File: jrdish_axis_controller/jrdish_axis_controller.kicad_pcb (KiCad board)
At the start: 4 copper layers, 85 x 80 mm, 168 parts, among them CN1 KF2EDGR-2.54-9P, CN10 KF2EDGR-2.54-4P, CN11 KF2EDGR-2.54-4P, CN12 KF2EDGR-2.54-2P, CN13 KF2EDGR-2.54-2P, CN2 KF2EDGR-2.54-6P, CN3 KF2EDGR-2.54-9P, CN4 KF2EDGR-2.54-6P, CN5 KF2EDGR-2.54-3P, CN6 KF2EDGR-2.54-2P, CN7 SM04B-SRSS-TB (LF)(SN), CN8 SM04B-SRSS-TB (LF)(SN), CN9 KF2EDGR-2.54-4P, J1 Conn_ARM_SWD_TagConnect_TC2030, M1 MountingHole_2.7mm_M2.5_ISO14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, Q1 AO3407A, Q2 AO3400A, Q3 2N7002, SW1 DSHP04TSGER, SW2 SS-12F49-G050, U1 STM32G474RET6, U2 ISOW1432BDFMR, U3 ISOW1432BDFMR, U4 MP2322GQH-Z, U5 LTC4311ISC6#TRPBF, U6 LM75BIMX-5/NOPB, U7 W25Q32JVSSIQ_C179173, U8 SP3232EEY-L/TR, X1 NX2016SA-16MHZ-EXS00A-CS07826

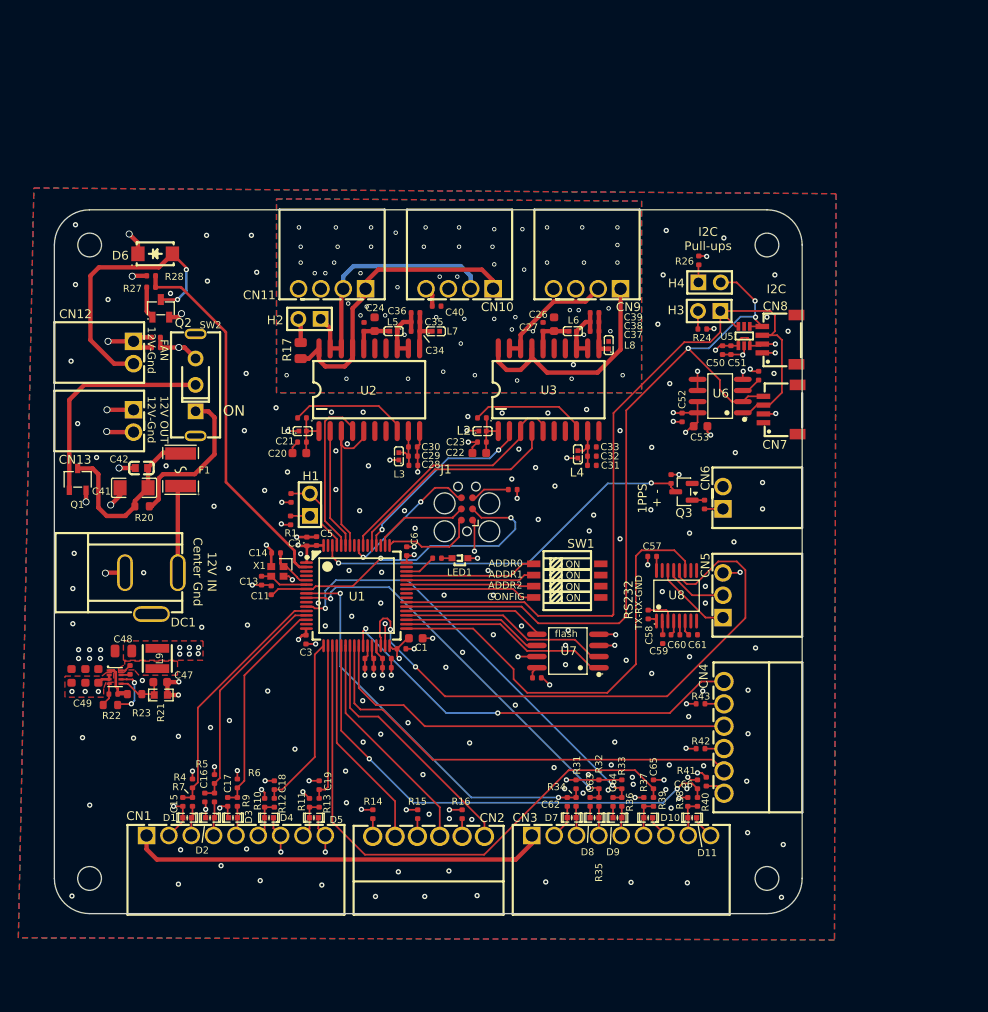
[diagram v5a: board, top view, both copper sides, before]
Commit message: RS485 isolated areas in place
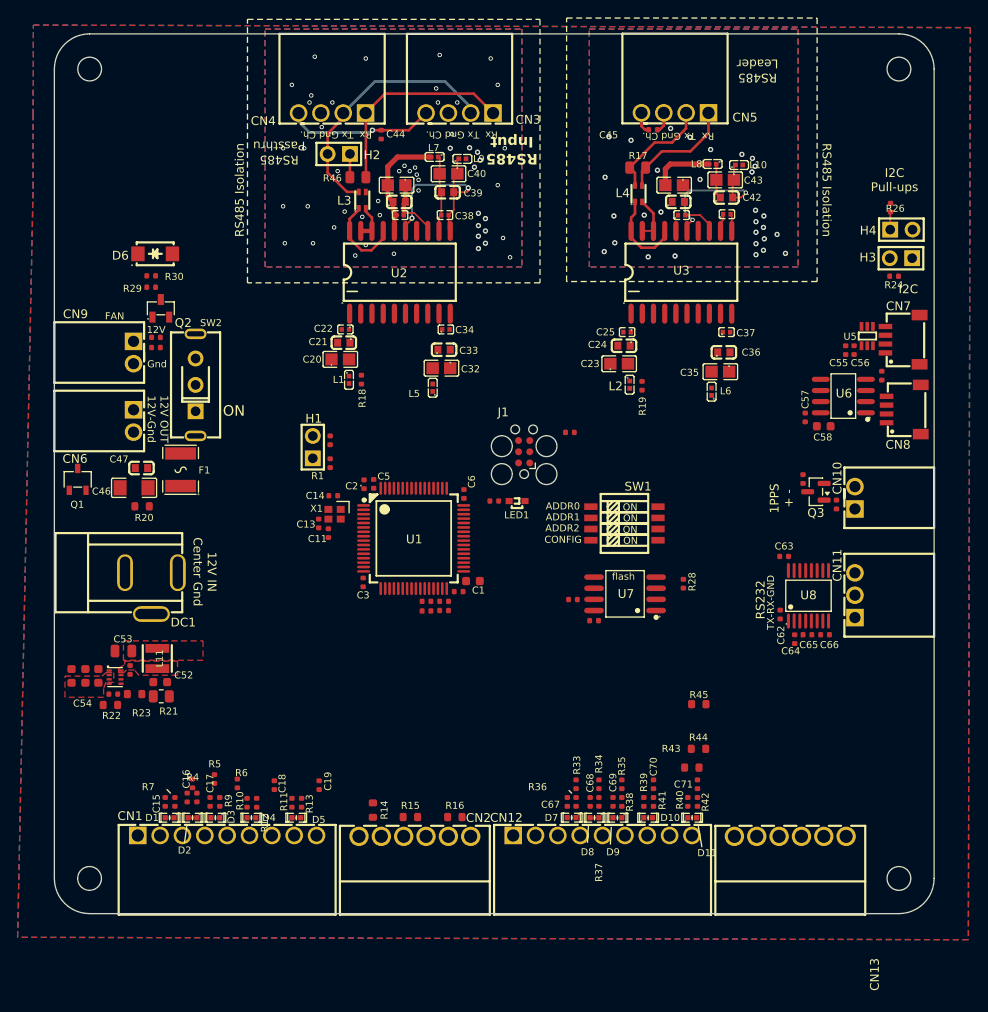
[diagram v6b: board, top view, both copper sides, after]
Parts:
- removed the CN4 at (191.5, 112.6)
- removed the R41 at (189.5, 117.6)
- removed the R42 at (188.8, 113.8)
- added C40: 10uF, MyParts:C0805, F.Cu at (160.2, 48.5)
- added C41: 10nF, MyParts:C0402, F.Cu at (191.8, 53.1)
- added C42: 1uF, MyParts:C0603, F.Cu at (191.8, 51.2)
- added C43: 10uF, MyParts:C0805, F.Cu at (191.7, 49.2)
- added C45: 10nF, PCM_JLCPCB:C_0402, F.Cu at (183.4, 43.5)
- added CN13: KF2EDGR-2.54-6P, MyParts:CONN-TH_KF2EDGR-2.54-6P, F.Cu at (199.1, 123.8)
- added L10: BLM15EX331SN1D, MyParts:L0402, F.Cu at (193.2, 47.5)
- added L3: Choke, MyParts:FILTER-SMD_4P-L2.0-W1.2-BL, F.Cu at (150.4, 51.5)
- added R27: 10kΩ, PCM_JLCPCB:R_0402, F.Cu at (174.3, 96.9)
- added R28: 10kΩ, PCM_JLCPCB:R_0402, F.Cu at (186.9, 95.1)
- added R44: 270Ω, PCM_JLCPCB:R_0603, F.Cu at (188.6, 113.9)
- added R45: 270Ω, PCM_JLCPCB:R_0603, F.Cu at (188.7, 108.8)
- added R46: 120Ω, PCM_JLCPCB:R_0805, F.Cu at (149.9, 48.9)
- C20: footprint PCM_JLCPCB:C_0603 -> MyParts:C0805
- C21, C27: value 100nF -> 1uF; footprint PCM_JLCPCB:C_0402 -> MyParts:C0603
- C22, C26: value 10uF -> .1uF; footprint PCM_JLCPCB:C_0603 -> MyParts:C0402
- C23: value 100nF -> 10uF; footprint PCM_JLCPCB:C_0402 -> MyParts:C0805
- C24: value 10uF -> 1uF; footprint PCM_JLCPCB:C_0603 -> MyParts:C0603
- C25: value 100nF -> .1uF; footprint PCM_JLCPCB:C_0402 -> MyParts:C0402
- C28, C31: value 10nF -> 10uF; footprint PCM_JLCPCB:C_0402 -> MyParts:C0805
- C29: value 1uF -> .1uF; footprint PCM_JLCPCB:C_0402 -> MyParts:C0402
- C30, C33, C36, C39: value 10nF -> 1uF; footprint PCM_JLCPCB:C_0402 -> MyParts:C0603
- C32, C35: value 1uF -> 10uF; footprint PCM_JLCPCB:C_0402 -> MyParts:C0805
- C34, C37: footprint PCM_JLCPCB:C_0402 -> MyParts:C0402
- C38: value 1uF -> 10nF; footprint PCM_JLCPCB:C_0402 -> MyParts:C0402
- L4: value BLM15EX331SN1D -> Choke; footprint MyParts:L0402 -> MyParts:FILTER-SMD_4P-L2.0-W1.2-BL
- R14, R15, R16, R43: value 330Ω -> 270Ω; footprint PCM_JLCPCB:R_0402 -> PCM_JLCPCB:R_0603
- R21: value 976Ω -> 976kΩ; footprint MyParts:R0603 -> Resistor_SMD:R_0805_2012Metric
- moved R17 43.6 mm to (181.7, 47.8), turned to 180 degrees
- moved C30 41.1 mm to (186.3, 51.7)
- moved C29 41.0 mm to (186.7, 53.2)
- moved C36 35.3 mm to (191.5, 68.8)
- moved C35 35.1 mm to (191.1, 71.0), turned to 180 degrees
- moved C31 33.2 mm to (185.8, 49.8), turned to 180 degrees
- moved C28 31.9 mm to (154.3, 49.8), turned to 180 degrees
- moved L4 30.4 mm to (181.8, 50.8), turned to 0 degrees
- moved C25 29.9 mm to (180.5, 66.5), turned to 180 degrees
- moved C24 28.5 mm to (180.2, 68.0), turned to 180 degrees
- moved M1 25.0 mm to (211.4, 36.6)
- moved L8 23.7 mm to (190.2, 47.4), turned to 180 degrees
- moved H4 22.6 mm to (211.7, 54.9)
- moved H3 22.6 mm to (211.6, 58.1)
- moved R24 22.6 mm to (210.8, 60.1)
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- renumbered C40 to C44, C41 to C46, C42 to C47, C43 to C48, C44 to C49, C45 to C50, C46 to C51, C47 to C52, C48 to C53, C49 to C54, C50 to C55, C51 to C56, C52 to C57, C53 to C58, C54 to C59, C55 to C60, C56 to C61, C58 to C62, C57 to C63, C59 to C64, C60 to C65, C61 to C66, C62 to C67, C63 to C68, C64 to C69, C65 to C70, C66 to C71, CN6 to CN10, CN5 to CN11, CN3 to CN12, CN10 to CN3, CN11 to CN4, CN9 to CN5, CN13 to CN6, CN8 to CN7, CN7 to CN8, CN12 to CN9, L9 to L11, L3 to L5, L5 to L7, L7 to L9, R27 to R29, R28 to R30, R29 to R31, R30 to R32, R31 to R33, R32 to R34, R33 to R35, R34 to R36, R35 to R37, R36 to R38, R37 to R39, R38 to R40, R39 to R41, R40 to R42
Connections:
- C20 pad 1: Net-(U2-VIO) -> GND
- C20 pad 2: GND -> Net-(U2-VIO)
- C22 pad 1: Net-(U3-VIO) -> Net-(U2-VIO)
- C23 pad 1: Net-(U3-VIO) -> GND
- C23 pad 2: GND -> Net-(U3-VIO)
- C24 pad 1: Net-(U2-VISOIN) -> Net-(U3-VIO)
- C24 pad 2: RS485_GND -> GND
- C25 pad 1: Net-(U2-VISOIN) -> Net-(U3-VIO)
- C25 pad 2: RS485_GND -> GND
- C26 pad 1: Net-(U3-VISOIN) -> Net-(U2-VISOIN)
- C26 pad 2: RS485_GND -> RS485_1_GND
- C27 pad 1: Net-(U3-VISOIN) -> Net-(U2-VISOIN)
- C27 pad 2: RS485_GND -> RS485_1_GND
- C28 pad 1: Net-(U2-VDD) -> RS485_1_GND
- C28 pad 2: GND -> Net-(U2-VISOIN)
- C29 pad 1: Net-(U2-VDD) -> Net-(U3-VISOIN)
- C29 pad 2: GND -> RS485_2_GND
- C30 pad 1: Net-(U2-VDD) -> Net-(U3-VISOIN)
- C30 pad 2: GND -> RS485_2_GND
- C31 pad 1: Net-(U3-VDD) -> RS485_2_GND
- C31 pad 2: GND -> Net-(U3-VISOIN)
- C32 pad 1: Net-(U3-VDD) -> GND
- C32 pad 2: GND -> Net-(U2-VDD)
- C33 pad 1: Net-(U3-VDD) -> Net-(U2-VDD)
- C34 pad 1: Net-(U2-MODE) -> Net-(U2-VDD)
- C34 pad 2: Net-(U2-GND2) -> GND
- C35 pad 1: Net-(U2-MODE) -> GND
- C35 pad 2: Net-(U2-GND2) -> Net-(U3-VDD)
- C36 pad 1: Net-(U2-MODE) -> Net-(U3-VDD)
- C36 pad 2: Net-(U2-GND2) -> GND
- C37 pad 1: Net-(U3-MODE) -> Net-(U3-VDD)
- C37 pad 2: Net-(U3-GND2) -> GND
- C38 pad 1: Net-(U3-MODE) -> Net-(U2-VISOOUT)
- C38 pad 2: Net-(U3-GND2) -> Net-(U2-GISOIN)
- C39 pad 1: Net-(U3-MODE) -> Net-(U2-VISOOUT)
- C39 pad 2: Net-(U3-GND2) -> Net-(U2-GISOIN)
- C44 pad 1: RS485_GND -> RS485_1_GND
- C44 pad 2: /RS485/RS485_CHASSIS -> /RS485/RS485_1_CHASSIS
- C59 pad 2: Net-(U7-VCC) -> GND
- C63 pad 2: Net-(U8-VCC) -> GND
- CN3 pad 1: /RS485/RS485_1_TX -> /RS485/RS485_1_RX
- CN3 pad 2: /RS485/RS485_1_RX -> /RS485/RS485_1_TX
- CN3 pad 3: RS485_GND -> RS485_1_GND
- CN3 pad 4: /RS485/RS485_CHASSIS -> /RS485/RS485_1_CHASSIS
- CN4 pad 1: /RS485/RS485_1_TX -> /RS485/RS485_1_RX
- CN4 pad 2: /RS485/RS485_1_RX -> /RS485/RS485_1_TX
- CN4 pad 3: RS485_GND -> RS485_1_GND
- CN4 pad 4: unconnected-(CN11-Pad4) -> /RS485/RS485_1_CHASSIS
- CN5 pad 1: /RS485/RS485_2_TX -> /RS485/RS485_2_RX
- CN5 pad 2: /RS485/RS485_2_RX -> /RS485/RS485_2_TX
- CN5 pad 3: RS485_GND -> RS485_2_GND
- CN5 pad 4: unconnected-(CN9-Pad4) -> /RS485/RS485_2_CHASSIS
- H2 pad 1: /RS485/RS485_1_RX -> Net-(H2-Pad1)
- H2 pad 2: Net-(H2-Pad2) -> /RS485/RS485_1_TX
- L1 pad 1: 3V3 -> Net-(U2-VIO)
- L1 pad 2: Net-(U2-VIO) -> 3V3
- L2 pad 1: 3V3 -> Net-(U3-VIO)
- L2 pad 2: Net-(U3-VIO) -> 3V3
- L4 pad 1: 3V3 -> Net-(U3-A)
- L4 pad 2: Net-(U3-VDD) -> Net-(U3-B)
- L6 pad 1: Net-(U3-MODE) -> 3V3
- L6 pad 2: Net-(U3-VISOIN) -> Net-(U3-VDD)
- L7 pad 1: Net-(U2-MODE) -> Net-(U2-VISOOUT)
- L8 pad 1: Net-(U3-GND2) -> Net-(U3-VISOOUT)
- L8 pad 2: RS485_GND -> Net-(U3-VISOIN)
- L9 pad 1: Net-(U2-GND2) -> Net-(U2-GISOIN)
- L9 pad 2: RS485_GND -> RS485_1_GND
- Q1 pad 2: 12V -> /Power/12V_IN_FUSED
- Q1 pad 3: /Power/12V_IN_FUSED -> 12V
- R17 pad 1: Net-(H2-Pad2) -> /RS485/RS485_2_RX
- R17 pad 2: /RS485/RS485_1_TX -> /RS485/RS485_2_TX
- R21 pad 1: Net-(U4-FB) -> 3V3
- R21 pad 2: 3V3 -> Net-(U4-FB)
- U2 pad 11: Net-(U2-GND2) -> Net-(U2-GISOIN)
- U2 pad 12: Net-(U2-MODE) -> Net-(U2-VISOOUT)
- U2 pad 13: Net-(U2-MODE) -> RS485_1_GND
- U2 pad 15: RS485_GND -> Net-(U2-GISOIN)
- U2 pad 17: /RS485/RS485_1_TX -> Net-(U2-A)
- U2 pad 18: /RS485/RS485_1_RX -> Net-(U2-B)
- U2 pad 19: /RS485/RS485_1_RX -> Net-(U2-B)
- U2 pad 20: /RS485/RS485_1_TX -> Net-(U2-A)
- U3 pad 11: Net-(U3-GND2) -> Net-(U3-GISOIN)
- U3 pad 12: Net-(U3-MODE) -> Net-(U3-VISOOUT)
- U3 pad 13: Net-(U3-MODE) -> RS485_2_GND
- U3 pad 15: RS485_GND -> Net-(U3-GISOIN)
- U3 pad 17: /RS485/RS485_2_TX -> Net-(U3-A)
- U3 pad 18: /RS485/RS485_2_RX -> Net-(U3-B)
- U3 pad 19: /RS485/RS485_2_RX -> Net-(U3-B)
- U3 pad 20: /RS485/RS485_2_TX -> Net-(U3-A)
- U7 pad 3: GND -> Net-(U7-WP#(IO2))
- U7 pad 7: GND -> Net-(U7-I03)
- U7 pad 8: Net-(U7-VCC) -> 3V3
- U8 pad 16: Net-(U8-VCC) -> 3V3
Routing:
- net GND: track 111.4 -> 0.00 mm, vias 193 -> 0
- net SDA_MCU: track 91.9 -> 0.00 mm
- net SCL_MCU: track 89.9 -> 0.00 mm, vias 3 -> 0
- net 3V3: track 78.1 -> 0.00 mm, vias 46 -> 0
- net RS232_RX_MCU: track 68.7 -> 0.00 mm, vias 2 -> 0
- net 12V: track 64.0 -> 0.00 mm, vias 7 -> 0
- net LIMIT2_SW1_MCU: track 63.9 -> 0.00 mm
- net LIMIT2_SW2_MCU: track 55.7 -> 0.00 mm, vias 2 -> 0
- net PUL2_MCU: track 51.7 -> 0.00 mm
- net RS232_TX_MCU: track 50.9 -> 0.00 mm
- net ENC2_Z_MCU: track 50.2 -> 0.00 mm, vias 2 -> 0
- net ENABLE2_MCU: track 48.5 -> 0.00 mm, vias 2 -> 0
- net DIR2_MCU: track 48.1 -> 0.00 mm
- net ENC2_A_MCU: track 46.1 -> 0.00 mm, vias 2 -> 0
- net ENC2_B_MCU: track 45.8 -> 0.00 mm, vias 2 -> 0
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- added copper zone on B.Cu, net RS485_1_GND
- added copper zone on F.Cu, net RS485_1_GND
- added copper zone on In1.Cu, net RS485_1_GND
- added copper zone on In2.Cu, net RS485_1_GND
- added copper zone on B.Cu, net RS485_2_GND
- added copper zone on F.Cu, net RS485_2_GND
- added copper zone on In1.Cu, net RS485_2_GND
- added copper zone on In2.Cu, net RS485_2_GND
- removed copper zone on B.Cu, net RS485_GND
- removed copper zone on F.Cu, net RS485_GND
- removed copper zone on In1.Cu, net RS485_GND
- removed copper zone on In2.Cu, net RS485_GND
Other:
- board size 85 x 80 mm -> 100 x 100 mm
- board text added: "FAN"
- board text added: "RS485 Input"
- board text added: "RS485 Isolation"
- board text added: "RS485 Leader"
- board text added: "RS485 Passthru"
- board text added: "Rx Tx Gnd Ch."
- board text removed: "12V Out"
- board text removed: "Dir+"
- board text removed: "Dir-"
- board text removed: "Enc 12V"
- board text removed: "Enc Gnd"
- board text removed: "EncA"
- board text removed: "EncB"
- board text removed: "EncZ"
- board text removed: "FAN 12V-Gnd"
- board text removed: "Lim1 Out"
- board text removed: "Lim1 Ret"
- board text removed: "Lim2 In"
- board text removed: "Lim2 Out"
- board text removed: "MF+"
- board text removed: "MF-"
- board text removed: "Pul+"
- board text removed: "Pul-"

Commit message: Near finished routing
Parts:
- added C72: 100nF, PCM_JLCPCB:C_0402, F.Cu at (202.6, 114.2)
- added C73: 100nF, PCM_JLCPCB:C_0402, F.Cu at (202.6, 112.7)
- added C74: 100nF, PCM_JLCPCB:C_0402, F.Cu at (202.6, 107.5)
- added C75: 100nF, PCM_JLCPCB:C_0402, F.Cu at (202.6, 106.3)
- added CN14: KF2EDGR-2.54-6P, MyParts:CONN-TH_KF2EDGR-2.54-6P, F.Cu at (206.3, 109.9)
- added D12: TPESD0402G05V, MyParts:D0402-BI, F.Cu at (204.2, 114.8)
- added D13: TPESD0402G05V, MyParts:D0402-BI, F.Cu at (204.2, 111.7)
- added D14: TPESD0402G05V, MyParts:D0402-BI, F.Cu at (204.2, 108.1)
- added D15: TPESD0402G05V, MyParts:D0402-BI, F.Cu at (204.2, 104.9)
- added R47: 4.7kΩ, PCM_JLCPCB:R_0402, F.Cu at (202.6, 116.4)
- added R48: 100Ω, PCM_JLCPCB:R_0402, F.Cu at (202.6, 115.3)
- added R49: 4.7kΩ, PCM_JLCPCB:R_0402, F.Cu at (202.6, 111.7)
- added R50: 100Ω, PCM_JLCPCB:R_0402, F.Cu at (202.6, 110.8)
- added R51: 4.7kΩ, PCM_JLCPCB:R_0402, F.Cu at (202.6, 109.7)
- added R52: 100Ω, PCM_JLCPCB:R_0402, F.Cu at (202.6, 108.6)
- added R53: 4.7kΩ, PCM_JLCPCB:R_0402, F.Cu at (202.6, 104.3)
- added R54: 100Ω, PCM_JLCPCB:R_0402, F.Cu at (202.6, 105.3)
- moved R45 18.4 mm to (202.0, 121.5)
- moved R44 11.4 mm to (196.9, 121.7)
- moved R43 6.99 mm to (191.9, 121.7)
- moved H3 5.50 mm to (211.6, 52.6)
- moved H4 5.50 mm to (211.7, 49.4)
- moved R24 5.50 mm to (210.8, 54.6)
- moved R26 5.50 mm to (210.4, 46.8)
- moved C58 4.90 mm to (202.8, 72.3)
- moved R25 4.90 mm to (209.4, 66.5)
- moved U5 4.90 mm to (207.8, 62.0)
- moved C55 4.90 mm to (205.3, 63.6)
- moved C56 4.90 mm to (206.3, 63.6)
- moved CN7 4.90 mm to (211.8, 62.5)
- moved CN8 4.90 mm to (211.9, 70.4)
- moved U6 4.90 mm to (205.1, 68.9)
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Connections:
- U1 pad 10: unconnected-(U1-PC2-Pad10) -> USER_SW_1_MCU
- U1 pad 4: unconnected-(U1-PC15-OSC32_OUT-Pad4) -> USER_SW_4_MCU
- U1 pad 40: unconnected-(U1-PC8-Pad40) -> USER_SW_2_MCU
- U1 pad 41: unconnected-(U1-PC9-Pad41) -> USER_SW_3_MCU
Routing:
- net USER_SW_1_MCU: track 0.00 -> 70.5 mm, vias 0 -> 2
- net ENABLE2_MCU: track 0.00 -> 66.8 mm, vias 0 -> 2
- net 3V3: track 0.00 -> 66.2 mm, vias 0 -> 46
- net USER_SW_4_MCU: track 0.00 -> 63.4 mm, vias 0 -> 2
- net SCL_MCU: track 0.00 -> 59.5 mm, vias 0 -> 2
- net DIR2_MCU: track 0.00 -> 58.8 mm
- net SDA_MCU: track 0.00 -> 57.4 mm
- net PUL2_MCU: track 0.00 -> 55.6 mm
- net RS485_2_DE_MCU: track 0.00 -> 50.4 mm, vias 0 -> 2
- net 1PPS_MCU: track 0.00 -> 50.2 mm, vias 0 -> 2
- net USER_SW_2_MCU: track 0.00 -> 49.8 mm, vias 0 -> 2
- net USER_SW_3_MCU: track 0.00 -> 49.3 mm, vias 0 -> 2
- net RS232_RX_MCU: track 0.00 -> 49.3 mm, vias 0 -> 2
- net FAN_MCU: track 0.00 -> 45.6 mm, vias 0 -> 2
- net ENC2_B_MCU: track 0.00 -> 45.4 mm, vias 0 -> 2
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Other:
- board text added: "1 G 2 3 G 4"
- board text added: "12V IN - 1Amp Center Gnd"
- board text added: "12V Out"
- board text added: "Axis 1"
- board text added: "Axis 2"
- board text added: "DIR+"
- board text added: "DIR-"
- board text added: "EN+"
- board text added: "EN-"
- board text added: "ENCA"
- board text added: "ENCB"
- board text added: "ENCZ"
- board text added: "LIM_SW1"
- board text added: "LIM_SW2"
- board text added: "PUL+"
- board text added: "PUL-"
- board text added: "Prog."
- board text added: "RS485 PINS Rx-Tx-Gnd-Chassis"
- board text added: "Tx Rx Gnd"
- board text added: "User Switches"
- board text removed: "12V IN Center Gnd"
- board text removed: "Rx Tx Gnd Ch."
- board text removed: "TX-RX-GND"

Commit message: Layout complete
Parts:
- added D16: TPESD0402G05V, MyParts:D0402-BI, F.Cu at (188.2, 93.2)
- added D17: TPESD0402G05V, MyParts:D0402-BI, F.Cu at (192.2, 93.3)
- added H5: 210S-1*3P L=11.6MMGold-plated black, MyParts:HDR-TH_3P-P2.54-V-M-1, F.Cu at (188.2, 88.7)
- added H6: 210S-1*3P L=11.6MMGold-plated black, MyParts:HDR-TH_3P-P2.54-V-M-1, F.Cu at (192.2, 88.7)
- added R55: 1kΩ, PCM_JLCPCB:R_0402, F.Cu at (188.2, 94.4)
- added R56: 1kΩ, PCM_JLCPCB:R_0402, F.Cu at (192.2, 94.5)
- moved C57 3.40 mm to (200.7, 72.8)
- moved CN10 1.49 mm to (206.4, 80.4)
- moved Q3 1.49 mm to (198.9, 79.8)
- moved R31 1.49 mm to (197.3, 81.3)
- moved R32 1.49 mm to (201.2, 81.2)
- moved R50 1.05 mm to (202.6, 111.8)
- moved R49 0.90 mm to (202.6, 110.8)
- moved C73 0.20 mm to (202.6, 112.9)
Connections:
- CN11 pad 1: Net-(U8-T1OUT) -> Net-(CN11-Pad1)
- CN11 pad 2: Net-(U8-R1IN) -> Net-(CN11-Pad2)
- U8 pad 13: Net-(U8-R1IN) -> /GPS RS232/R1IN
- U8 pad 14: Net-(U8-T1OUT) -> /GPS RS232/T1OUT
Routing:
- net 12V: track 12.6 -> 62.5 mm, vias 6 -> 7
- net SCL_MCU: track 59.5 -> 91.4 mm, vias 2 -> 5
- net SDA_MCU: track 57.4 -> 89.0 mm
- net Net-(CN11-Pad1): track 0.00 -> 21.5 mm, vias 0 -> 1
- net 3V3: track 66.2 -> 85.0 mm, vias 46 -> 58
- net Net-(U8-T1OUT): track 18.5 -> 0.00 mm
- net Net-(R20-Pad2): track 0.00 -> 17.6 mm, vias 0 -> 1
- net Net-(CN11-Pad2): track 0.00 -> 17.4 mm
- net /GPS RS232/T1OUT: track 0.00 -> 12.7 mm
- net Net-(U8-R1IN): track 11.4 -> 0.00 mm
- net GND: track 16.7 -> 26.3 mm, vias 81 -> 249
- net RS232_RX_MCU: track 49.3 -> 58.7 mm
- net /GPS RS232/R1IN: track 0.00 -> 8.81 mm
- net Net-(U3-VIO): track 1.83 -> 9.72 mm
- net Net-(U4-PG): track 0.00 -> 6.15 mm, vias 0 -> 2
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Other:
- board text added: "C34"
